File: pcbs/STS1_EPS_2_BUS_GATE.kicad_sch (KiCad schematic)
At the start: 17 parts, among them Q2 SI7135DP-T1-GE3, Q3 SI7135DP-T1-GE3, Q4 SI7135DP-T1-GE3, Q5 SI7135DP-T1-GE3, U27 TPS2420RSAT

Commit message: worked on sts1_eps_1
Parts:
- added Q22: SI7135DP-T1-GE3, STS_Package_SO:POWERPAK_SO8_single, symbol STS_Transistor_FET:SI7135DP-T1-GE3
- added R26: 100k, Resistor_SMD:R_0805_2012Metric, symbol Device:R
- added R27: 0, Resistor_SMD:R_0805_2012Metric, symbol Device:R
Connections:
- net VOUT_GATED: now also Q22.5, R27.2; no longer Q4.5, R11.2
- new net: Q22.1, Q22.2, Q22.3, Q4.5, R11.2, R26.1, R27.1
- new net UVLO_SIGNAL: Q22.4, R26.2
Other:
- note added: "Undervoltage Lockout"

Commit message: Worked on STS1_EPS_2.
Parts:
- renumbered C29 to C2, Q3 to Q5, Q22 to Q6, Q5 to Q7, Q2 to Q8, Q4 to Q9, R38 to R12, R39 to R13, R40 to R14, R37 to R15, R26 to R16, R42 to R17, R27 to R18, R41 to R19, R1 to R20, R8 to R21, R9 to R22, R10 to R23, R11 to R24, U27 to U3

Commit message: Worked on STS1_EPS_2.
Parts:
- removed Q6, Q7, Q8, Q9: SI7135DP-T1-GE3, STS_Package_SO:POWERPAK_SO8_single, symbol STS_Transistor_FET:SI7135DP-T1-GE3
- removed R16, R19, R21, R23: 100k, Resistor_SMD:R_0805_2012Metric, symbol Device:R
- removed R18, R20, R22, R24: 0, Resistor_SMD:R_0805_2012Metric, symbol Device:R
- added Q6: 2N7002, Package_TO_SOT_SMD:SOT-23, symbol Transistor_FET:2N7002
- added TP18, TP26: TestPoint, TestPoint:TestPoint_THTPad_D1.0mm_Drill0.5mm, symbol Connector:TestPoint
- added U10: 4072, Package_SO:SOIC-14_3.9x8.7mm_P1.27mm, symbol 4xxx:4072
- U3: footprint Package_DFN_QFN:VQFN-16-1EP_3x3mm_P0.5mm_EP1.45x1.45mm_ThermalVias -> STS_Package_DFN_QFN:QFN65P400X400X100-17N
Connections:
- net DS2_SIGNAL: now also U10.10
- net DT_SIGNAL: now also U10.2; no longer Q5.4, R15.2
- net GND: now also Q6.2 (S), U10.11, U10.12, U10.7 (VSS)
- net RBF_SIGNAL: now also U10.3
- net UVLO_SIGNAL: now also U10.5
- net VOUT_GATED: now also Q5.5, R17.2
- new net: Q6.1 (G), TP18.1, U10.13
- new net: U10.1, U10.9
- new net +5V: U10.14 (VDD)
- new net DS1_SIGNAL: U10.4
- new net GATE_SIGNAL: Q5.4, Q6.3 (D), R15.2, TP26.1
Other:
- note removed: "DS2"
- note removed: "DS2 Bypass (optional)"
- note removed: "DS3"
- note removed: "DS3 Bypass (optional)"
- note removed: "RBF"
- note removed: "RBF Bypass (optional)"
- note removed: "Undervoltage Lockout"

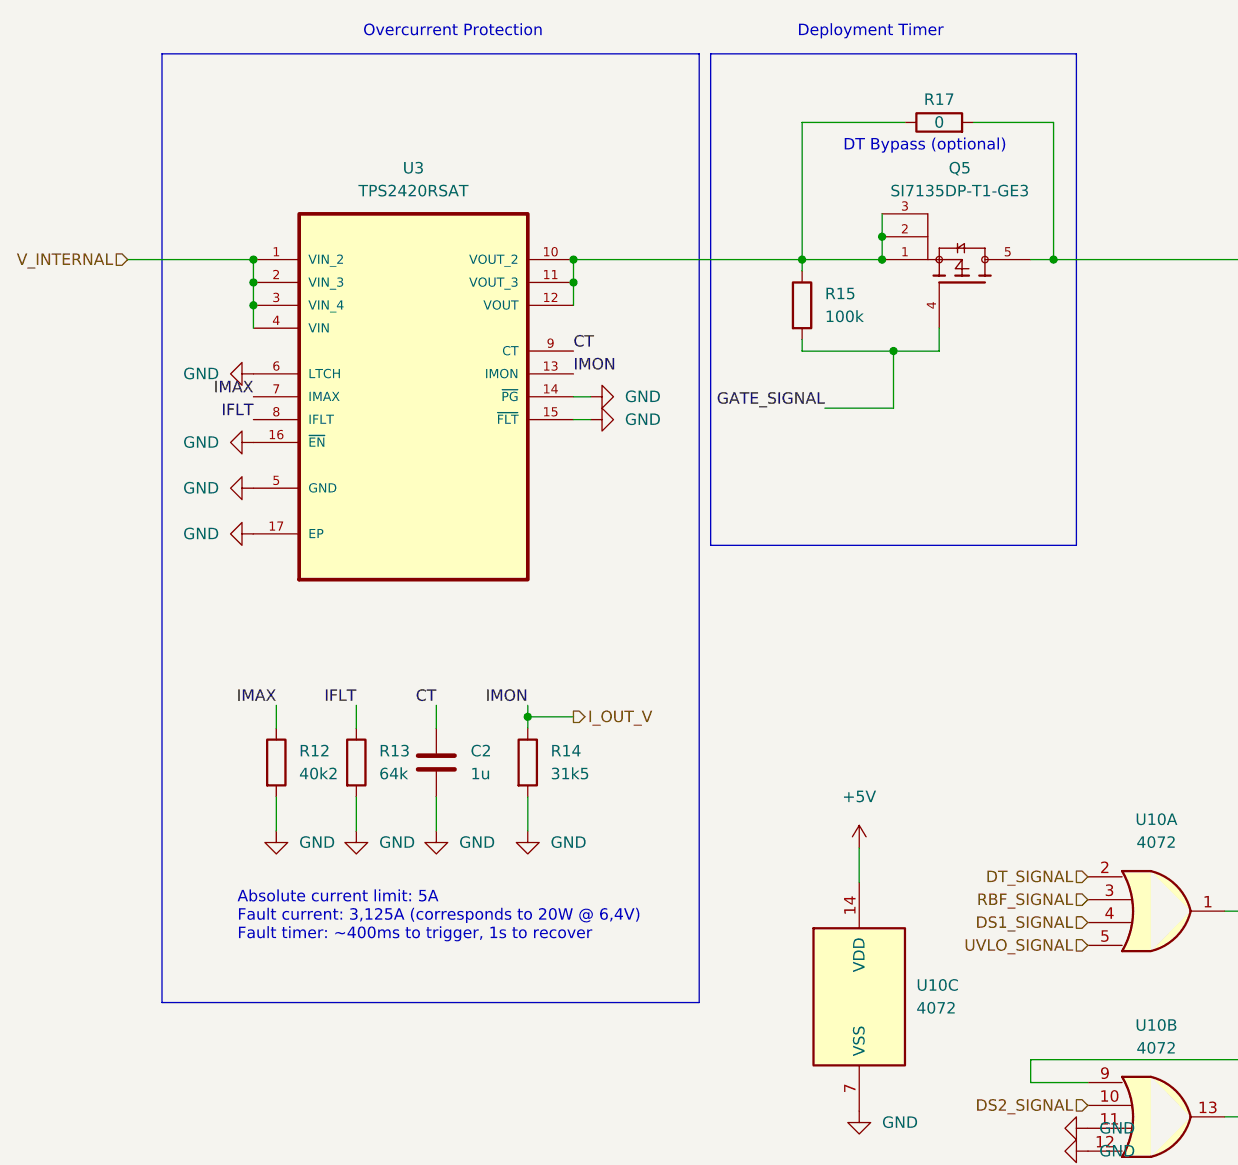
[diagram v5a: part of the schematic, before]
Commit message: Ported kicad projects to KiCad 8.0.
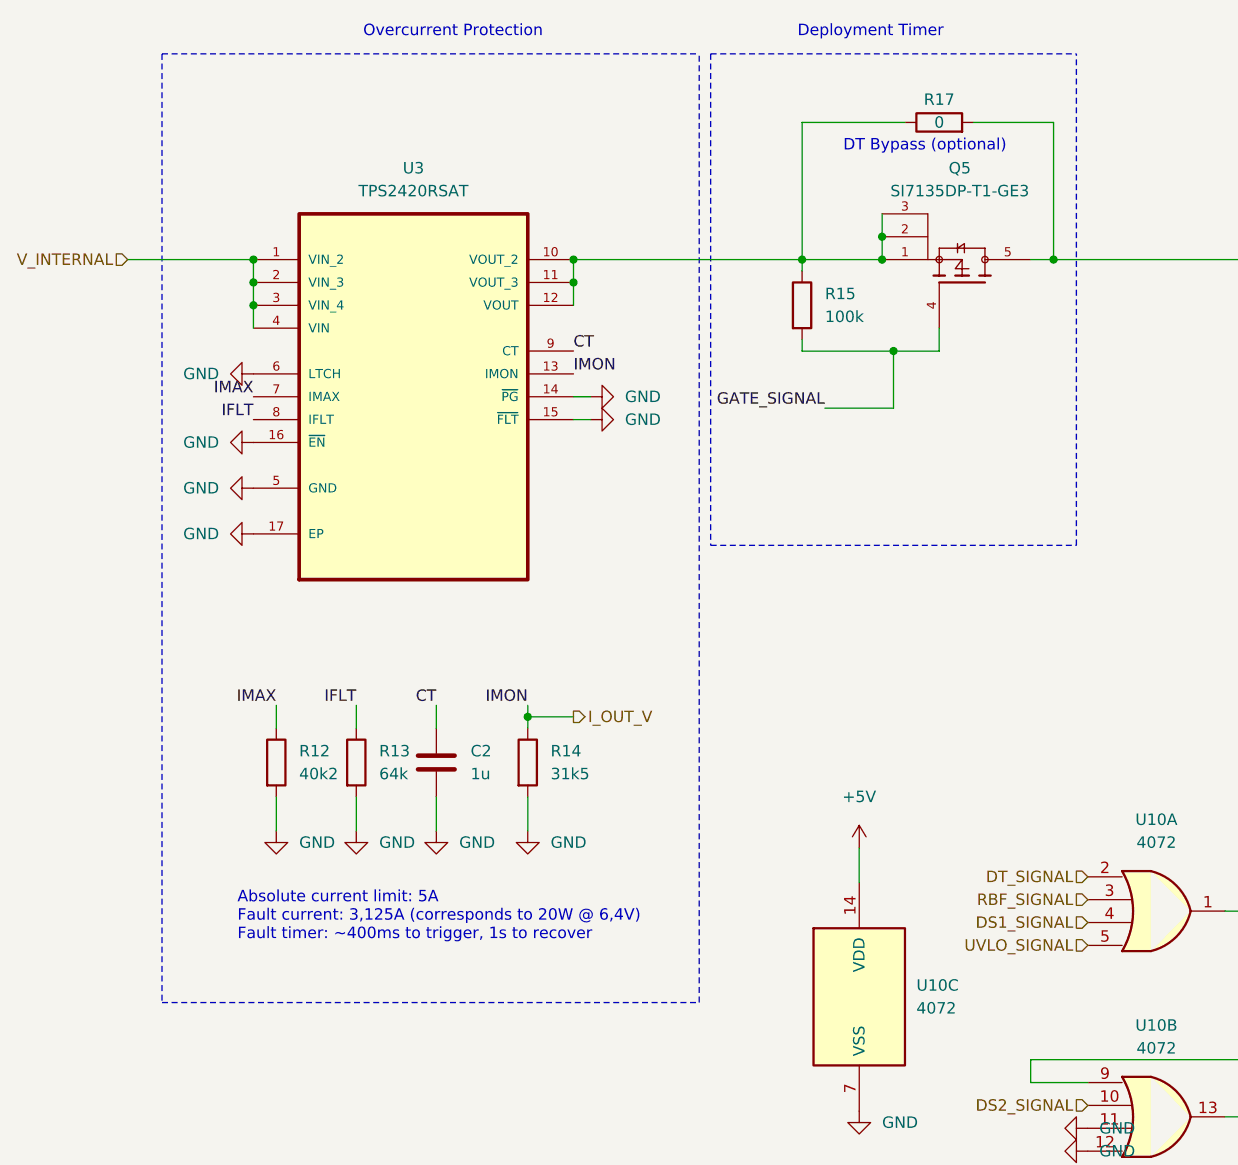
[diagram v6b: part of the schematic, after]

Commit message: Changed some footprints that had the wrong shape in EPS 2.1.
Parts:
- U10: footprint Package_SO:SOIC-14_3.9x8.7mm_P1.27mm -> STS_Misc:SOP127P780X200-14N
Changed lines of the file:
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@@
 			)
 		)
-		(property "Footprint" "Package_SO:SOIC-14_3.9x8.7mm_P1.27mm"
+		(property "Footprint" "STS_Misc:SOP127P780X200-14N"
 			(at 140.97 134.62 0)
 			(effects
@@
 			)
 		)
-		(property "Footprint" "Package_SO:SOIC-14_3.9x8.7mm_P1.27mm"
+		(property "Footprint" "STS_Misc:SOP127P780X200-14N"
 			(at 140.97 111.76 0)
 			(effects
@@
 			)
 		)
-		(property "Footprint" "Package_SO:SOIC-14_3.9x8.7mm_P1.27mm"
+		(property "Footprint" "STS_Misc:SOP127P780X200-14N"
 			(at 107.95 121.285 0)
 			(effects
